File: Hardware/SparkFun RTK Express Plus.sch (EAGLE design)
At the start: 109 parts, among them J13 Internal, J16 MICRO-SD-PUSH-PUSH-EXT-PIN, J17 Qwiic Right Angle, J20 FPC_12_0.5MM_BACKFLIP, J3 USB Female Type C Connector, J4 External, J5 USB Female Type C Connector, Q1 SIL2308-TP, Q2 MBT3904DW1T1, U1 74HC4052D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

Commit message: File rename
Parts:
- added R6, R8: 10k, SparkFun-Resistors:10KOHM-0603-1/10W-1%
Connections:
- removed net ESP_3V3: R34.2
- net 3.3V: now also R34.2, R6.2, R8.2
- net EXT_DIR: now also R6.1
- net EXT_WT: now also R8.1
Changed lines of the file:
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@@
 <part name="J16" library="SparkFun-Connectors" deviceset="MICRO-SD" device="-PUSH-PUSH-EXT-PIN"/>
 <part name="J15" library="SparkFun-Connectors" deviceset="CONN_02" device="1X02_NO_SILK"/>
+<part name="SUPPLY11" library="SparkFun-PowerSymbols" deviceset="3.3V" device=""/>
+<part name="R6" library="SparkFun-Resistors" deviceset="10KOHM" device="-0603-1/10W-1%" value="10k"/>
+<part name="R8" library="SparkFun-Resistors" deviceset="10KOHM" device="-0603-1/10W-1%" value="10k"/>
+<part name="SUPPLY40" library="SparkFun-PowerSymbols" deviceset="3.3V" device=""/>
+<part name="SUPPLY41" library="SparkFun-PowerSymbols" deviceset="3.3V" device=""/>
 </parts>
 <sheets>
@@
 <attribute name="NAME" x="73.66" y="130.048" size="1.778" layer="95" font="vector"/>
 </instance>
+<instance part="SUPPLY11" gate="G$1" x="322.58" y="104.14" smashed="yes">
+<attribute name="VALUE" x="322.58" y="106.934" size="1.778" layer="96" align="bottom-center"/>
+</instance>
 </instances>
 <busses>
@@
 <pinref part="U11" gate="G$1" pin="V_USB"/>
 </segment>
+<segment>
+<pinref part="R34" gate="G$1" pin="2"/>
+<pinref part="SUPPLY11" gate="G$1" pin="3.3V"/>
+<wire x1="322.58" y1="104.14" x2="322.58" y2="101.6" width="0.1524" layer="91"/>
+</segment>
 </net>
 <net name="GND" class="0">
@@
 <label x="203.2" y="27.94" size="1.27" layer="95" xref="yes"/>
 <pinref part="U5" gate="U1" pin="IA35"/>
-</segment>
-</net>
-<net name="ESP_3V3" class="1">
-<segment>
-<pinref part="R34" gate="G$1" pin="2"/>
-<wire x1="322.58" y1="101.6" x2="322.58" y2="104.14" width="0.1524" layer="91"/>
-<label x="322.58" y="104.14" size="1.27" layer="95" rot="R90" xref="yes"/>
 </segment>
 </net>
@@
 <wire x1="142.24" y1="177.8" x2="142.24" y2="279.4" width="0.2032" layer="97" style="longdash"/>
 <text x="198.12" y="266.7" size="2.54" layer="94" font="vector" align="center">Wheel Tick and Direction Signal</text>
-<text x="185.42" y="248.92" size="2.54" layer="97" font="vector" align="center">Schmitt Trigger Output</text>
+<text x="187.96" y="248.92" size="2.54" layer="97" font="vector" align="center">Schmitt Trigger Output</text>
 <text x="73.66" y="43.18" size="2.54" layer="97" font="vector" align="center">All input signals must be
 limited to 3.3V</text>
@@
 <attribute name="NAME" x="175.26" y="211.582" size="1.778" layer="95"/>
 <attribute name="VALUE" x="175.26" y="193.04" size="1.778" layer="95"/>
+</instance>
+<instance part="R6" gate="G$1" x="165.1" y="210.82" smashed="yes" rot="R90">
+<attribute name="NAME" x="163.576" y="210.82" size="1.778" layer="95" font="vector" rot="R90" align="bottom-center"/>
+<attribute name="VALUE" x="166.624" y="210.82" size="1.778" layer="96" font="vector" rot="R90" align="top-center"/>
+</instance>
+<instance part="R8" gate="G$1" x="165.1" y="238.76" smashed="yes" rot="R90">
+<attribute name="NAME" x="163.576" y="238.76" size="1.778" layer="95" font="vector" rot="R90" align="bottom-center"/>
+<attribute name="VALUE" x="166.624" y="238.76" size="1.778" layer="96" font="vector" rot="R90" align="top-center"/>
+</instance>
+<instance part="SUPPLY40" gate="G$1" x="165.1" y="246.38" smashed="yes">
+<attribute name="VALUE" x="165.1" y="249.174" size="1.778" layer="96" align="bottom-center"/>
+</instance>
+<instance part="SUPPLY41" gate="G$1" x="165.1" y="218.44" smashed="yes">
+<attribute name="VALUE" x="165.1" y="221.234" size="1.778" layer="96" align="bottom-center"/>
 </instance>
 </instances>
@@
 <wire x1="170.18" y1="210.82" x2="170.18" y2="208.28" width="0.1524" layer="91"/>
 <pinref part="U9" gate="U1" pin="VCC"/>
+</segment>
+<segment>
+<pinref part="R8" gate="G$1" pin="2"/>
+<pinref part="SUPPLY40" gate="G$1" pin="3.3V"/>
+<wire x1="165.1" y1="246.38" x2="165.1" y2="243.84" width="0.1524" layer="91"/>
+</segment>
+<segment>
+<pinref part="R6" gate="G$1" pin="2"/>
+<pinref part="SUPPLY41" gate="G$1" pin="3.3V"/>
+<wire x1="165.1" y1="218.44" x2="165.1" y2="215.9" width="0.1524" layer="91"/>
 </segment>
 </net>
@@
 </segment>
 <segment>
-<wire x1="172.72" y1="231.14" x2="170.18" y2="231.14" width="0.1524" layer="91"/>
-<label x="170.18" y="231.14" size="1.27" layer="95" font="vector" rot="R180" xref="yes"/>
+<wire x1="172.72" y1="231.14" x2="165.1" y2="231.14" width="0.1524" layer="91"/>
+<label x="160.02" y="231.14" size="1.27" layer="95" font="vector" rot="R180" xref="yes"/>
 <pinref part="U8" gate="U1" pin="A"/>
+<pinref part="R8" gate="G$1" pin="1"/>
+<wire x1="165.1" y1="231.14" x2="160.02" y2="231.14" width="0.1524" layer="91"/>
+<wire x1="165.1" y1="233.68" x2="165.1" y2="231.14" width="0.1524" layer="91"/>
+<junction x="165.1" y="231.14"/>
 </segment>
 </net>
@@
 </segment>
 <segment>
-<wire x1="172.72" y1="203.2" x2="170.18" y2="203.2" width="0.1524" layer="91"/>
-<label x="170.18" y="203.2" size="1.27" layer="95" font="vector" rot="R180" xref="yes"/>
+<wire x1="172.72" y1="203.2" x2="165.1" y2="203.2" width="0.1524" layer="91"/>
+<label x="160.02" y="203.2" size="1.27" layer="95" font="vector" rot="R180" xref="yes"/>
 <pinref part="U9" gate="U1" pin="A"/>
-</segment>
-</net>
+<pinref part="R6" gate="G$1" pin="1"/>
+<wire x1="165.1" y1="203.2" x2="160.02" y2="203.2" width="0.1524" layer="91"/>
+<wire x1="165.1" y1="205.74" x2="165.1" y2="203.2" width="0.1524" layer="91"/>
+<junction x="165.1" y="203.2"/>
+</segment>
+</net>

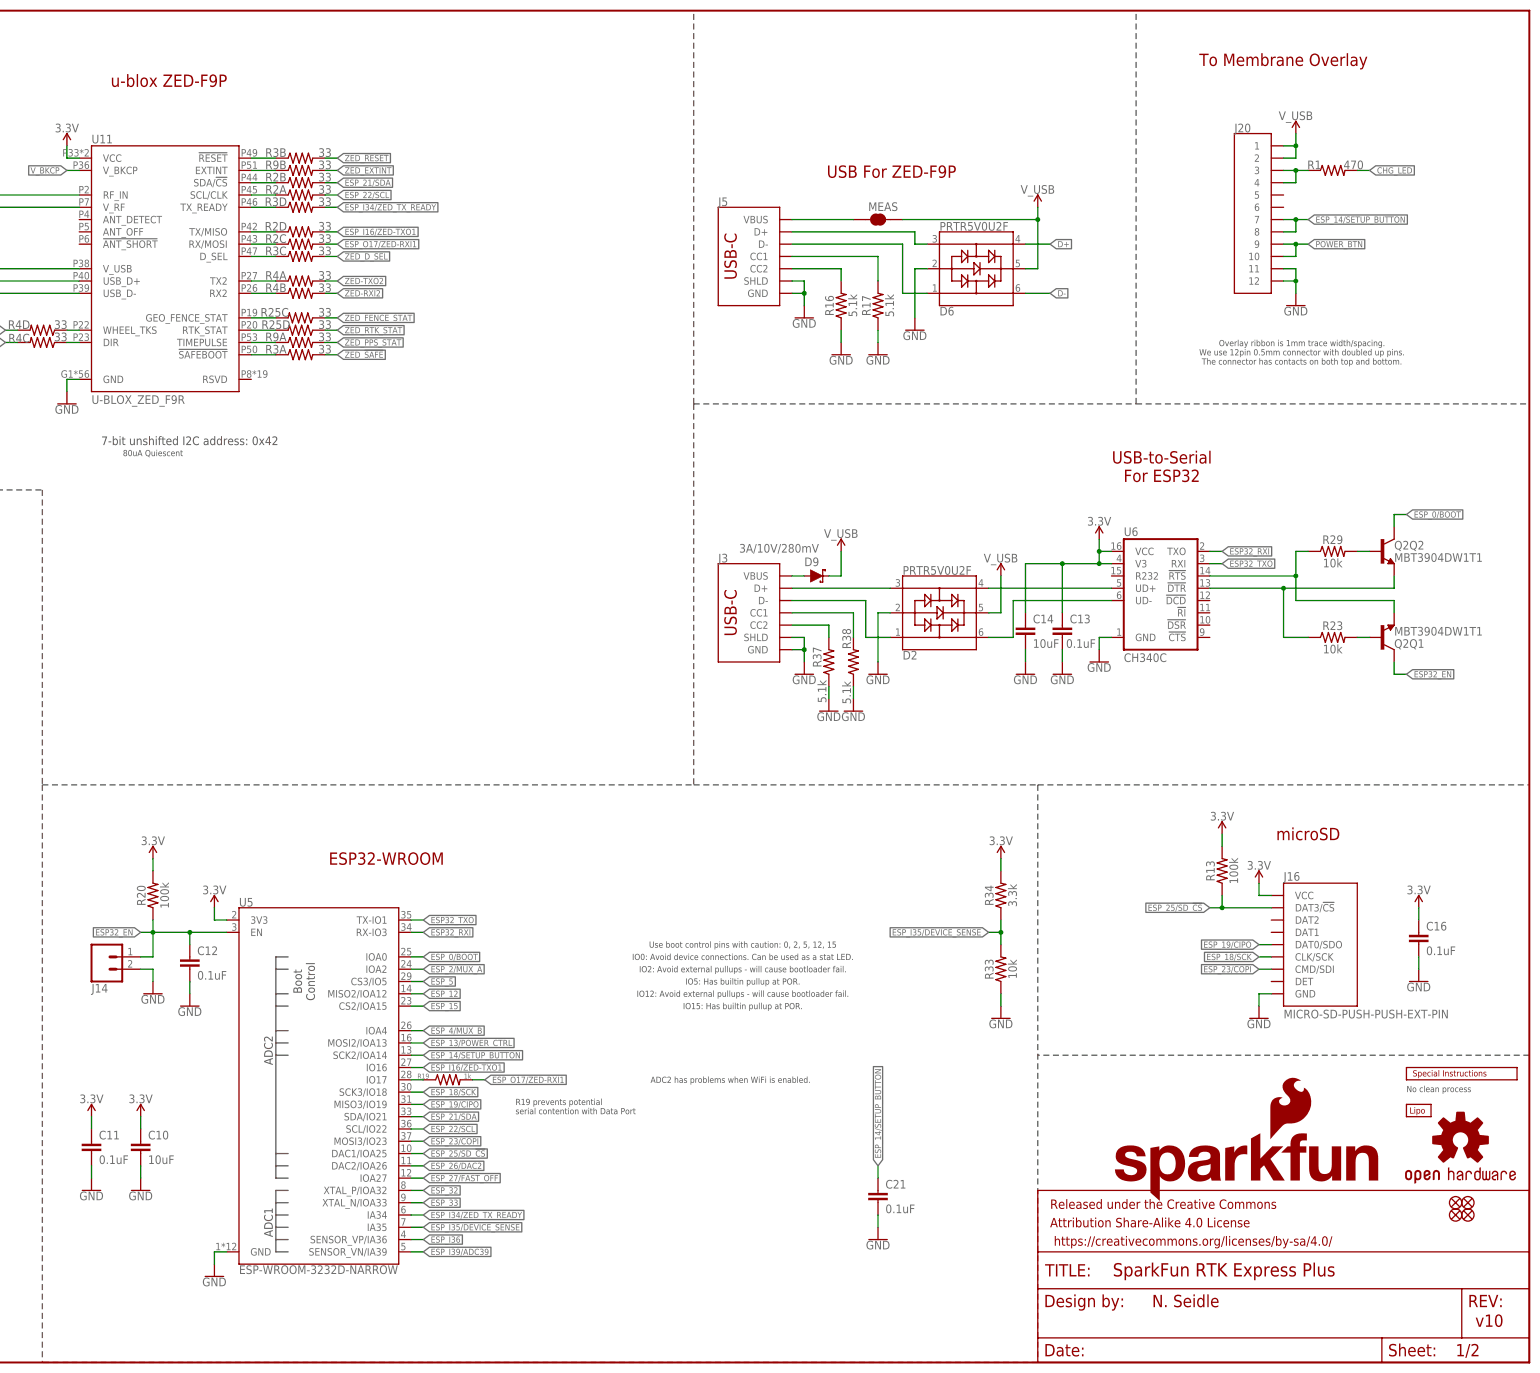
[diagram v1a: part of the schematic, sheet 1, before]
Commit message: Updating readme. Update version to v11 on schematic.
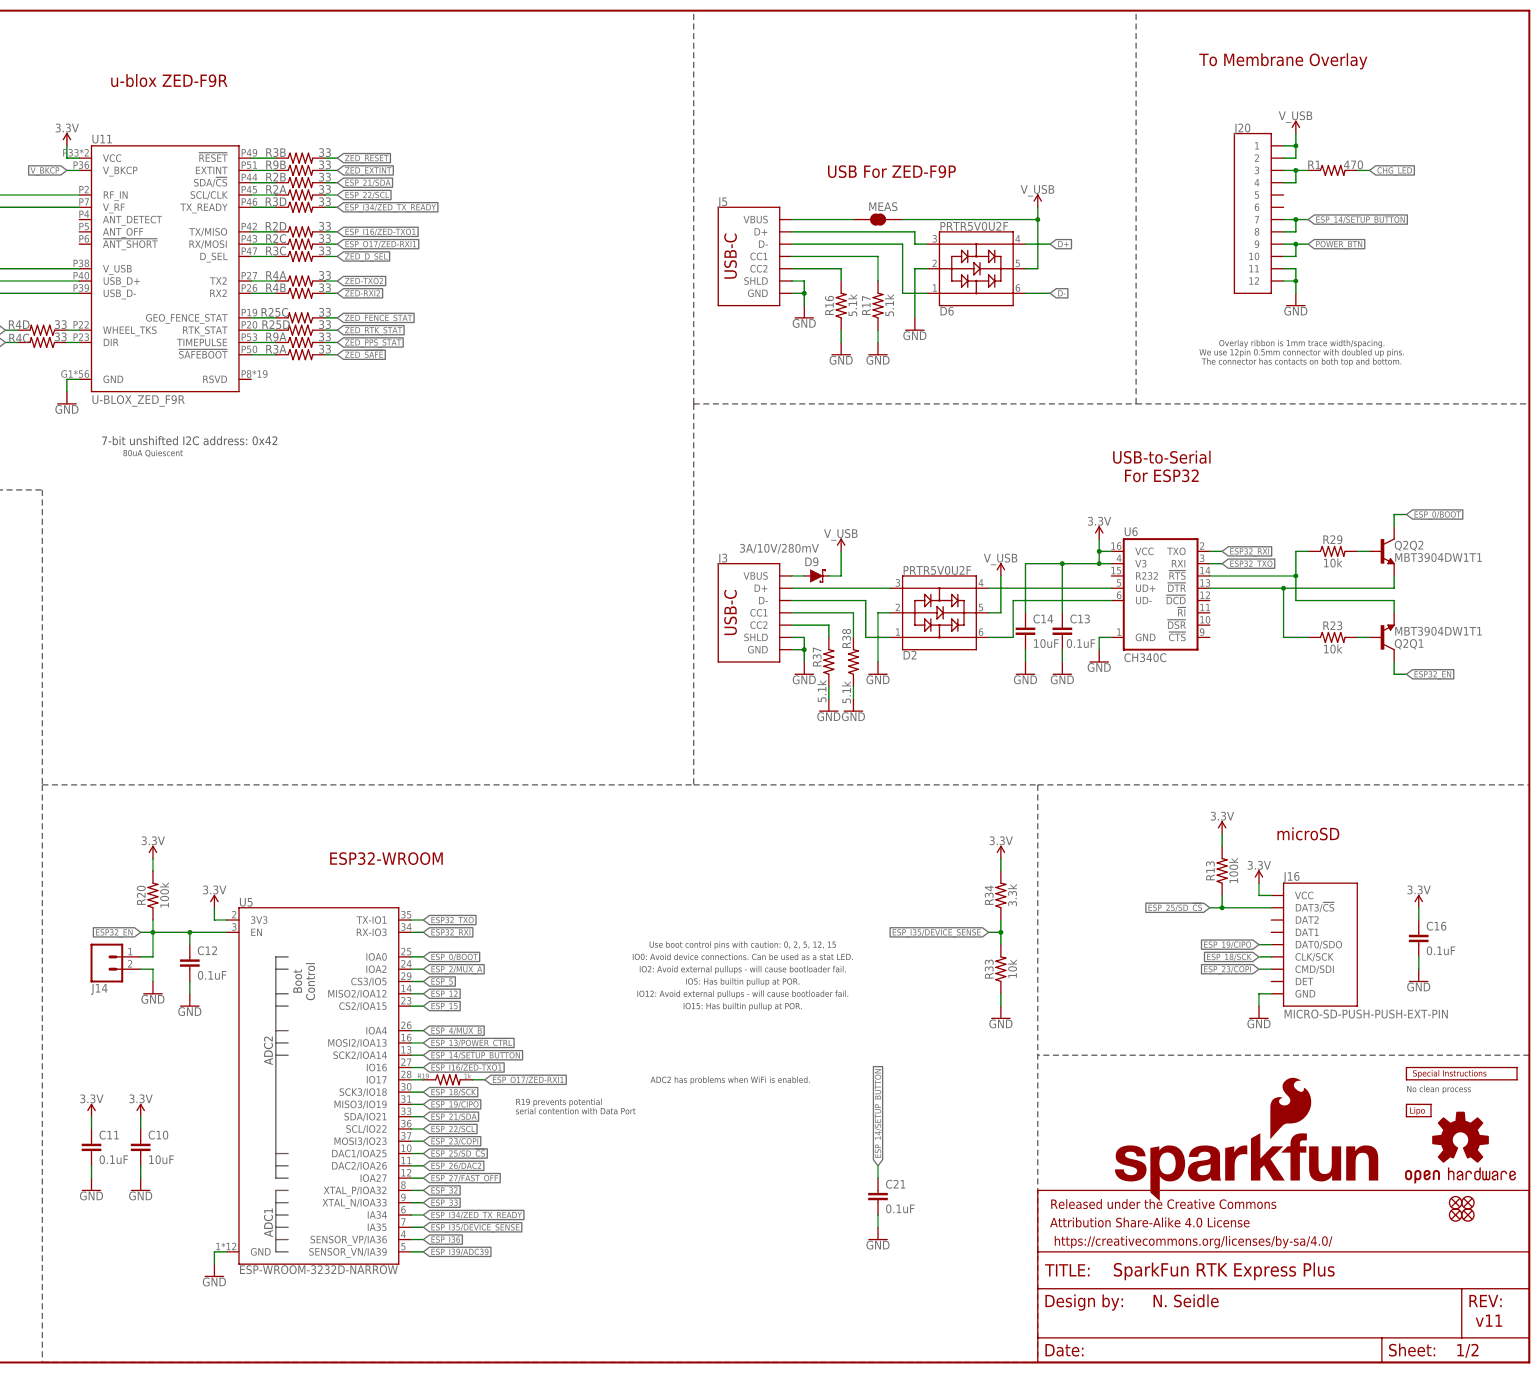
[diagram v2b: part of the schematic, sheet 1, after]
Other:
- note added: "u-blox ZED-F9R"
- note added: "v11"
- note removed: "u-blox ZED-F9P"
- note removed: "v10"
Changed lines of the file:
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@@
 <sheet>
 <plain>
-<text x="420.624" y="7.366" size="2.54" layer="94">v10</text>
+<text x="420.624" y="7.366" size="2.54" layer="94">v11</text>
 <text x="154.94" y="190.5" size="1.778" layer="97" align="center">7-bit unshifted I2C address: 0x42</text>
-<text x="150.622" y="264.922" size="2.54" layer="94" rot="MR180" align="center">u-blox ZED-F9P</text>
+<text x="150.622" y="264.922" size="2.54" layer="94" rot="MR180" align="center">u-blox ZED-F9R</text>
 <text x="47.752" y="243.84" size="1.778" layer="97">LQW15ANR12J00D</text>
 <text x="66.04" y="266.7" size="1.27" layer="97">Board thickness: 1.6mm</text>
@@
 limited to 3.3V</text>
 <wire x1="261.62" y1="177.8" x2="261.62" y2="279.4" width="0.2032" layer="97" style="longdash"/>
+<text x="423.164" y="7.366" size="2.54" layer="94">v11</text>
 </plain>
 <instances>
@@
 <attribute name="SHEET" x="416.56" y="1.27" size="2.54" layer="94" font="vector"/>
 <attribute name="DRAWING_NAME" x="345.694" y="17.78" size="2.7432" layer="94" font="vector"/>
-<attribute name="REV" x="419.1" y="6.604" size="2.7432" layer="94" font="vector"/>
 <attribute name="DESIGNER" x="353.314" y="11.176" size="2.7432" layer="94" font="vector"/>
 </instance>

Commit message: v13 PCB - LIF connector, accel ground plane, ESP32 FP.
* Removed ground plane from around the accel to aid in reflow and rework
* Route out text in screw areas
* New 6 pin overlay connector
* ENIG finish
* Full ESP32 FP
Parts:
- removed J20: FPC_12_0.5MM_BACKFLIP, RTK Facet:FPC_12_0.5MM_BACKFLIP
- added J19: (no value), SparkFun-Connectors:CONN_061MM-LIF
- D10: value PESD0402 -> PESD0402-0402; device SparkFun-DiscreteSemi:PESD0402 -> SparkFun-DiscreteSemi:PESD0402-0402
- U5: value ESP-WROOM-3232D-NARROW -> ESP-WROOM-3232D; device SparkFun-RF:ESP-WROOM-3232D-NARROW -> SparkFun-RF:ESP-WROOM-3232D
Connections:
- net CHG_LED_RES: now also J19.2; no longer J20.3, J20.4
- net ESP32_!DTR: now also Q2G2.E; no longer Q2Q2.E
- net ESP32_!RTS: now also Q2G1.E; no longer Q2Q1.E
- net ESP32_EN: now also Q2G1.C; no longer Q2Q1.C
- net ESP_0/BOOT: now also Q2G2.C; no longer Q2Q2.C
- net ESP_14/SETUP_BUTTON: now also J19.4; no longer J20.7, J20.8
- net GND: now also J19.6; no longer J20.11, J20.12
- net N$24: now also Q2G1.B; no longer Q2Q1.B
- net N$25: now also Q2G2.B; no longer Q2Q2.B
- net POWER_BTN: now also J19.5; no longer J20.10, J20.9
- net V_USB: now also J19.1; no longer J20.1, J20.2
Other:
- moved on the sheet: R1
